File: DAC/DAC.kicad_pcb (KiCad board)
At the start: 4 copper layers, 54 x 21.6 mm, 32 parts, among them J1 Conn_01x06, J2 Conn_01x06, U1 TPS73633DBV, U2 PCM5242RHB

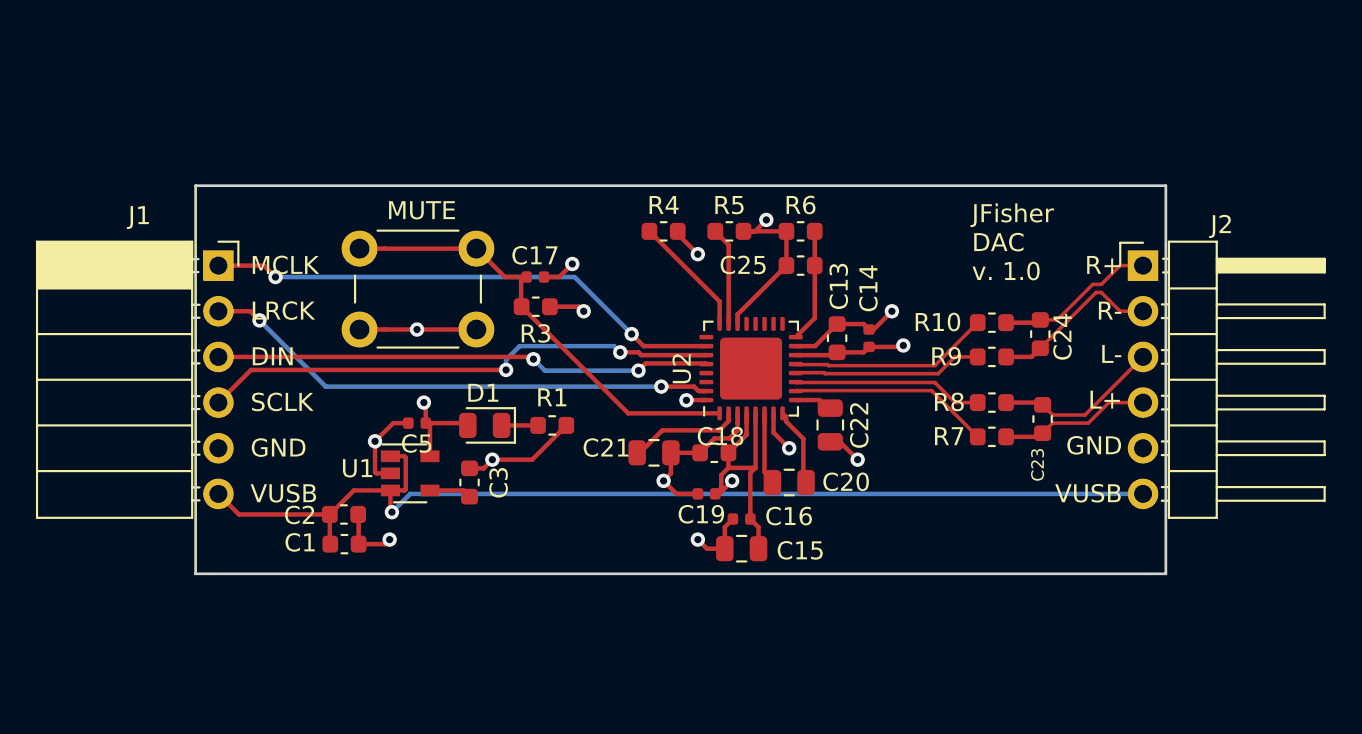
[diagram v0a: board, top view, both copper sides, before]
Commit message: Work around DAC incompatibility with I2S clock (#4)
* Update DAC to expose config pins and to use larger components

* Ignore some more cache & backup files

* Update PCB placement

* Add headers for MCLK/SCLK signal to allow for clock workaround

This helps to address the issue called out in the datasheet: https://e2e.ti.com/support/audio/f/6/p/804836/2980033#2980033, allowing the DAC to receive the MCLK input and create a usable SCLK input from it.
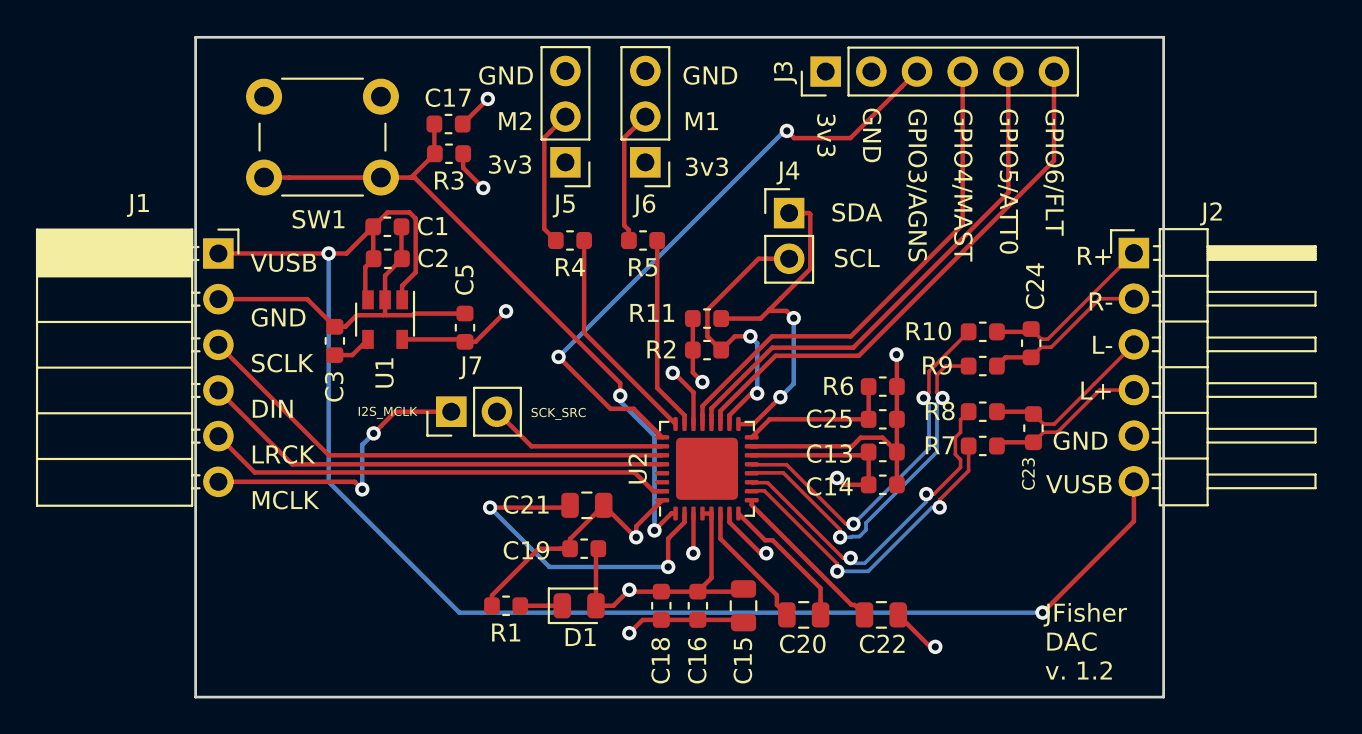
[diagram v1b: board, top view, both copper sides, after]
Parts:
- removed MUTE: SW_Push, Button_Switch_THT:SW_PUSH_6mm
- added J3: Conn_01x06_Male, Connector_PinHeader_2.54mm:PinHeader_1x06_P2.54mm_Vertical, F.Cu at (146.8, 34.3)
- added J4: Conn_01x02, Connector_PinHeader_2.54mm:PinHeader_1x02_P2.54mm_Vertical, F.Cu at (144.8, 42.2)
- added J5: Conn_01x03_Male, Connector_PinHeader_2.54mm:PinHeader_1x03_P2.54mm_Vertical, F.Cu at (132.3, 39.3)
- added J6: Conn_01x03_Male, Connector_PinHeader_2.54mm:PinHeader_1x03_P2.54mm_Vertical, F.Cu at (136.8, 39.3)
- added J7: Conn_01x02, Connector_PinHeader_2.54mm:PinHeader_1x02_P2.54mm_Vertical, F.Cu at (126.0, 53.2)
- added R11: 4.7k, Resistor_SMD:R_0603_1608Metric, F.Cu at (140.2, 48.0)
- added R2: 4.7k, Resistor_SMD:R_0603_1608Metric, F.Cu at (140.2, 49.8)
- added SW1: SW_Push, Button_Switch_THT:SW_PUSH_6mm, F.Cu at (115.6, 35.7)
- C14, C16, C17, C19, C5: footprint Capacitor_SMD:C_0402_1005Metric -> Capacitor_SMD:C_0603_1608Metric
- moved C1 17.8 mm to (122.4, 42.9)
- moved C2 14.4 mm to (122.5, 44.7)
- moved D1 11.3 mm to (133.1, 64.0), turned to 0 degrees
- moved C22 10.9 mm to (149.9, 64.5), turned to 0 degrees
- moved C3 10.9 mm to (119.5, 49.3)
- moved R1 10.4 mm to (129.0, 64.0), turned to 180 degrees
- moved C17 9.78 mm to (125.8, 37.2)
- moved R3 9.78 mm to (125.9, 38.9)
- moved R6 9.77 mm to (150.0, 51.8), turned to 180 degrees
- moved C25 9.70 mm to (150.0, 53.6), turned to 0 degrees
- moved C18 9.00 mm to (137.7, 64.0), turned to 270 degrees
- moved U1 8.67 mm to (122.3, 48.1), turned to 270 degrees
- moved C14 8.19 mm to (150.0, 57.3), turned to 0 degrees
- moved C19 7.46 mm to (133.4, 60.8)
- moved C20 7.41 mm to (145.6, 64.5)
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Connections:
- net Net-(R4-Pad1) renamed MODE2
- net Net-(R5-Pad1) renamed MODE1
- J1 pad 1: I2S_MCLK -> VUSB
- J1 pad 2: I2S_LRCK -> GND
- J1 pad 3: I2S_DIN -> I2S_SCLK
- J1 pad 4: I2S_SCLK -> I2S_DIN
- J1 pad 5: GND -> I2S_LRCK
- J1 pad 6: VUSB -> I2S_MCLK
- R4 pad 2: +3V3 -> Net-(J5-Pad2)
- R5 pad 2: GND -> Net-(J6-Pad2)
- U2 pad 17: (no net) -> SDA_MOSI_ATT2
- U2 pad 18: (no net) -> SCL_MC_ATT1
- U2 pad 19: (no net) -> GPIO5_ATT0
- U2 pad 20: (no net) -> GPIO4_MAST
- U2 pad 21: (no net) -> GPIO3_AGNS
- U2 pad 25: (no net) -> GPIO6_FLT
- U2 pad 26: I2S_MCLK -> I2S_SCK_SRC
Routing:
- net GPIO6_FLT: track 0.00 -> 34.5 mm, vias 0 -> 2
- net GPIO5_ATT0: track 0.00 -> 30.0 mm
- net GPIO4_MAST: track 0.00 -> 29.1 mm
- net GPIO3_AGNS: track 0.00 -> 28.2 mm
- net VUSB: track 59.2 -> 86.1 mm, vias 1 -> 2
- net SDA_MOSI_ATT2: track 0.00 -> 19.5 mm, vias 0 -> 2
- net SCL_MC_ATT1: track 0.00 -> 16.1 mm, vias 0 -> 2
- net Net-(C17-Pad1): track 24.8 -> 38.6 mm, vias 0 -> 2
- net GND: track 57.5 -> 70.5 mm, vias 12 -> 8
- net Net-(C21-Pad1): track 6.10 -> 19.1 mm, vias 0 -> 2
- net I2S_MCLK: track 29.0 -> 16.4 mm
- net OUTR_N: track 10.5 -> 20.7 mm, vias 0 -> 2
- net I2S_SCK_SRC: track 0.00 -> 9.99 mm
- net OUTR_P: track 11.1 -> 20.6 mm, vias 0 -> 2
- net +3V3: track 30.9 -> 40.0 mm
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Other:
- board size 54 x 21.6 mm -> 53.8 x 36.7 mm
- board text added: "3v3"
- board text added: "GPIO3/AGNS"
- board text added: "GPIO4/MAST"
- board text added: "GPIO5/ATT0"
- board text added: "GPIO6/FLT"
- board text added: "I2S_MCLK"
- board text added: "JFisher DAC v. 1.2"
- board text added: "M1"
- board text added: "M2"
- board text added: "SCK_SRC"
- board text added: "SCL"
- board text added: "SDA"
- board text removed: "JFisher DAC v. 1.0"
